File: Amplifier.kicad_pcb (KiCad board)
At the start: 2 copper layers, 68 x 50 mm, 28 parts, among them J1 Input, J2 Power, J3 Transformer, J4 Neon bulb, U1 6N2P, U2 6P14P

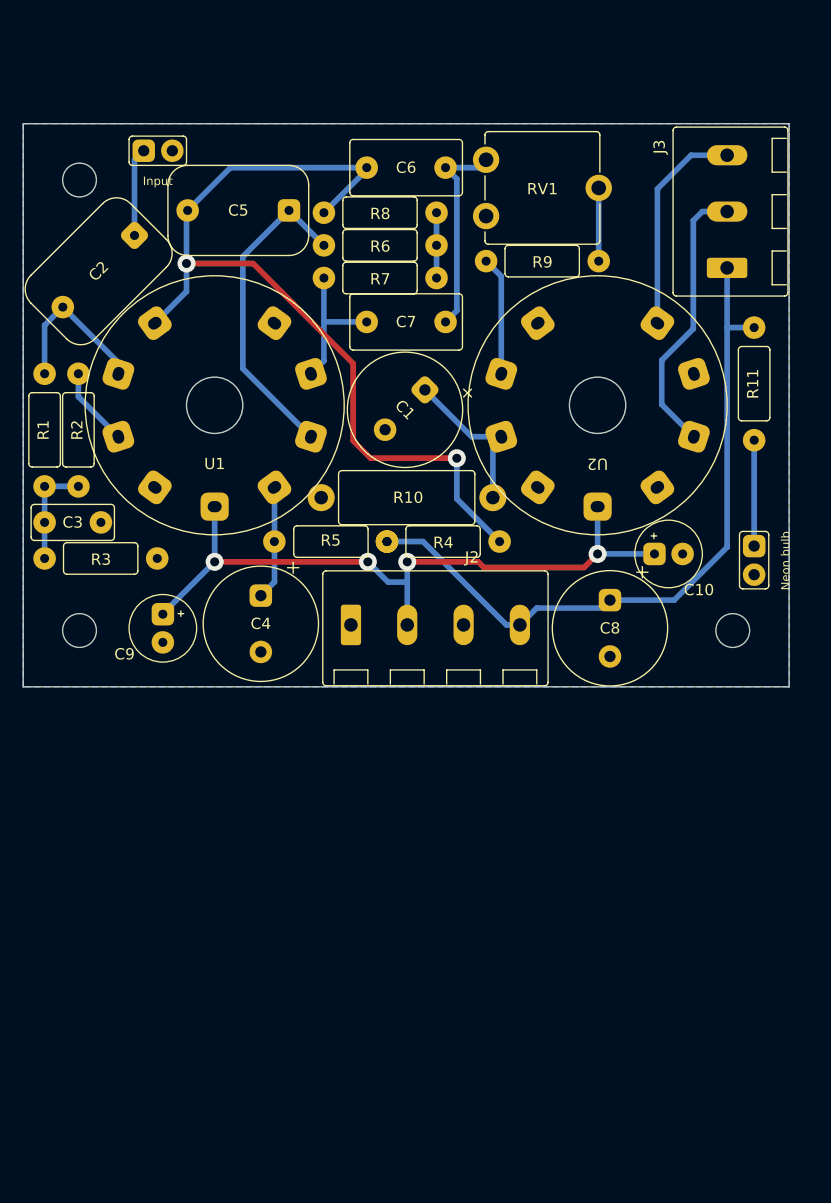
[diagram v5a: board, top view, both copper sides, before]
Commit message: More rounded corners!
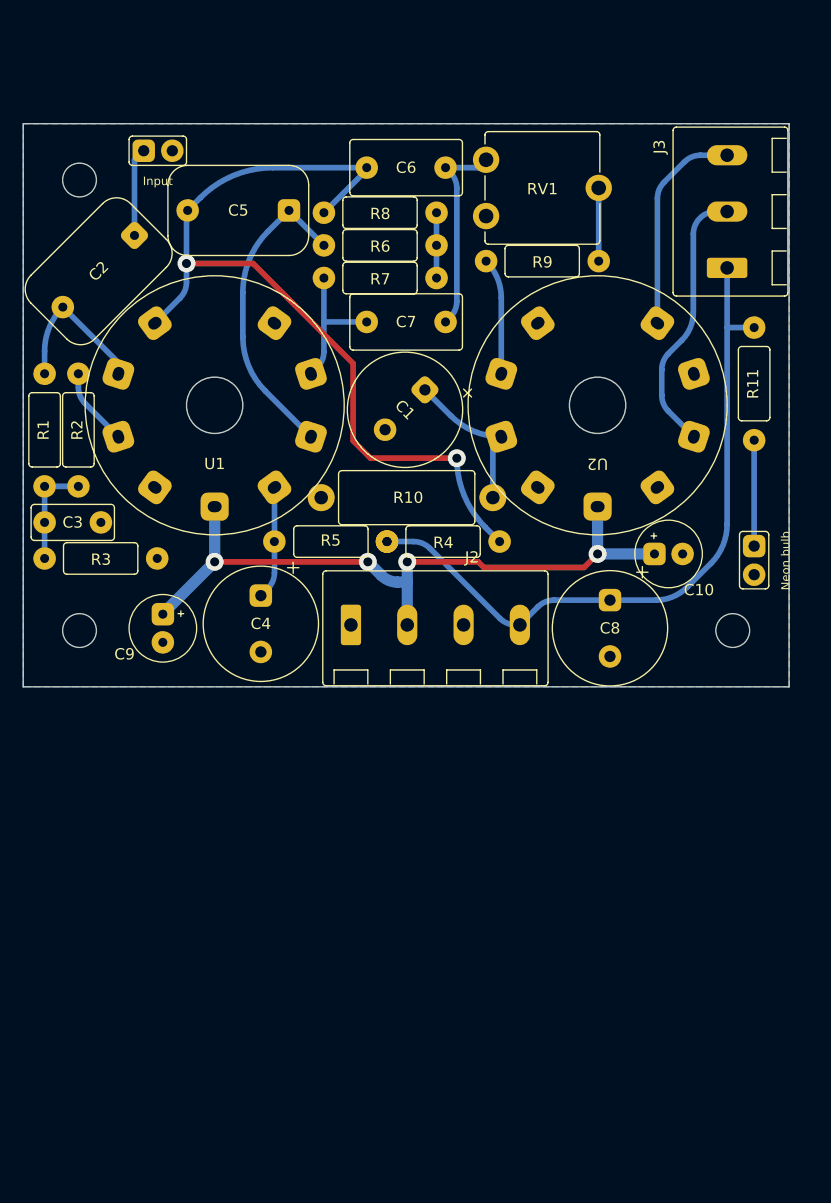
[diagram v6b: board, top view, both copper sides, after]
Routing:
- net 240V: track 63.6 -> 62.6 mm
- net Net-(C5-Pad2): track 78.4 -> 77.5 mm
- net Net-(U2-Pad7): track 24.9 -> 24.0 mm
- net Net-(C5-Pad1): track 28.7 -> 28.0 mm

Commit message: Hybrid Amplifier
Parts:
- added T1: Transformer_SP_1S, spdf1626_lib:Output_transformer, F.Cu at (91.3, 115.7)
- J3: value Transformer -> Output; footprint spdf1626_lib:MCV_1,5_4-G-5.0_1x03_P5.0mm_Vertical -> spdf1626_lib:PinHeader_1x02_P2.54mm
- moved J3 71.7 mm to (61.3, 96.8), turned to 0 degrees
- moved R11 37.1 mm to (89.5, 88.2), turned to 0 degrees
- moved J4 34.5 mm to (88.3, 91.9), turned to 90 degrees
- moved J2 25.4 mm to (118.9, 93.2), turned to -90 degrees
- moved C8 8.70 mm to (100.4, 92.0)
- moved C10 7.64 mm to (108.9, 90.6), turned to -90 degrees
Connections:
- J3 pad 1: 240V -> Net-(J3-Pin_1)
- J3 pad 2: Net-(U2-Pad7) -> GND
- U2 pad 7: Net-(U2-Pad7) -> Net-(T1-PM)
- U2 pad 9: Net-(U2-Pad9) -> Net-(T1-PR2)
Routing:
- net Net-(T1-PR2): track 0.00 -> 91.6 mm
- net Net-(J3-Pin_1): track 0.00 -> 59.9 mm
- net Net-(T1-PM): track 0.00 -> 51.4 mm
- net Net-(U2-Pad7): track 24.0 -> 0.00 mm
- net Net-(U2-Pad9): track 19.2 -> 0.00 mm
- net 240V: track 62.6 -> 53.3 mm
- net +6V: track 61.7 -> 67.7 mm, vias 4 -> 2
- net Net-(J4-Pin_1): track 9.40 -> 5.28 mm
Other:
- board size 68 x 50 mm -> 68 x 88 mm
